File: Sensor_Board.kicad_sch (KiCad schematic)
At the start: 0 parts

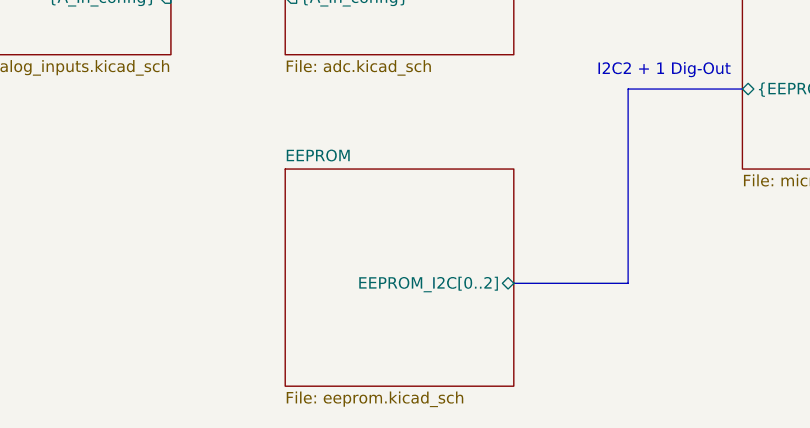
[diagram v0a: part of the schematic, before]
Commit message: added net-classes
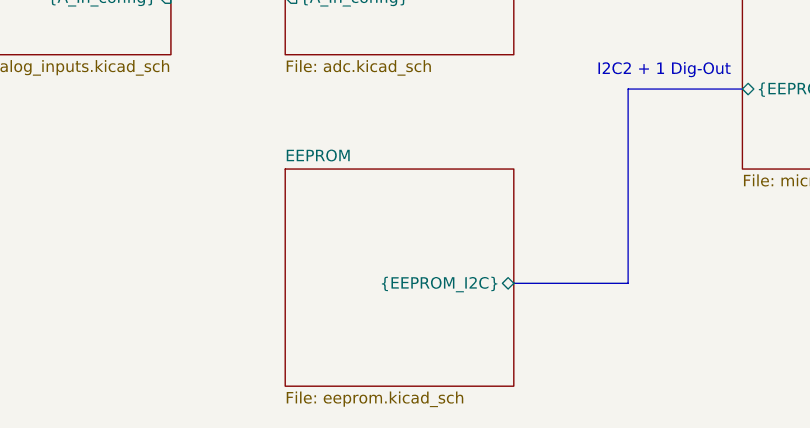
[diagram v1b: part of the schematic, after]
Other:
- sheet EEPROM ports: added {EEPROM_I2C}; removed EEPROM_I2C[0..2]
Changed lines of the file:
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@@
       (effects (font (size 1.27 1.27)) (justify left top))
     )
-    (pin "EEPROM_I2C[0..2]" bidirectional (at 152.4 165.1 0)
+    (pin "{EEPROM_I2C}" bidirectional (at 152.4 165.1 0)
       (effects (font (size 1.27 1.27)) (justify right))
     )

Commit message: completed schematic
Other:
- note removed: "ToDo: USB Transceivers Power Out Microcontroller"
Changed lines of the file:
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@@
-    (effects (font (size 1.27 1.27)) (justify left bottom))
-  )
-  (text "ToDo:\nUSB\nTransceivers\nPower Out\nMicrocontroller" (at 19.05 31.75 0)
     (effects (font (size 1.27 1.27)) (justify left bottom))
   )
